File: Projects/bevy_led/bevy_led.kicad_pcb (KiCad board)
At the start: 2 copper layers, 66 x 61 mm, 78 parts, among them J1 USB_C_Receptacle_USB2.0, SW1 SW_Push, SW2 SW_Push, SW3 SW_Push, SW4 SW_Push, U1 DRTR5V0U4S, U2 ESP32-S3-MINI-1, U3 74AHCT1G125, U4 XC6222B331MR-G

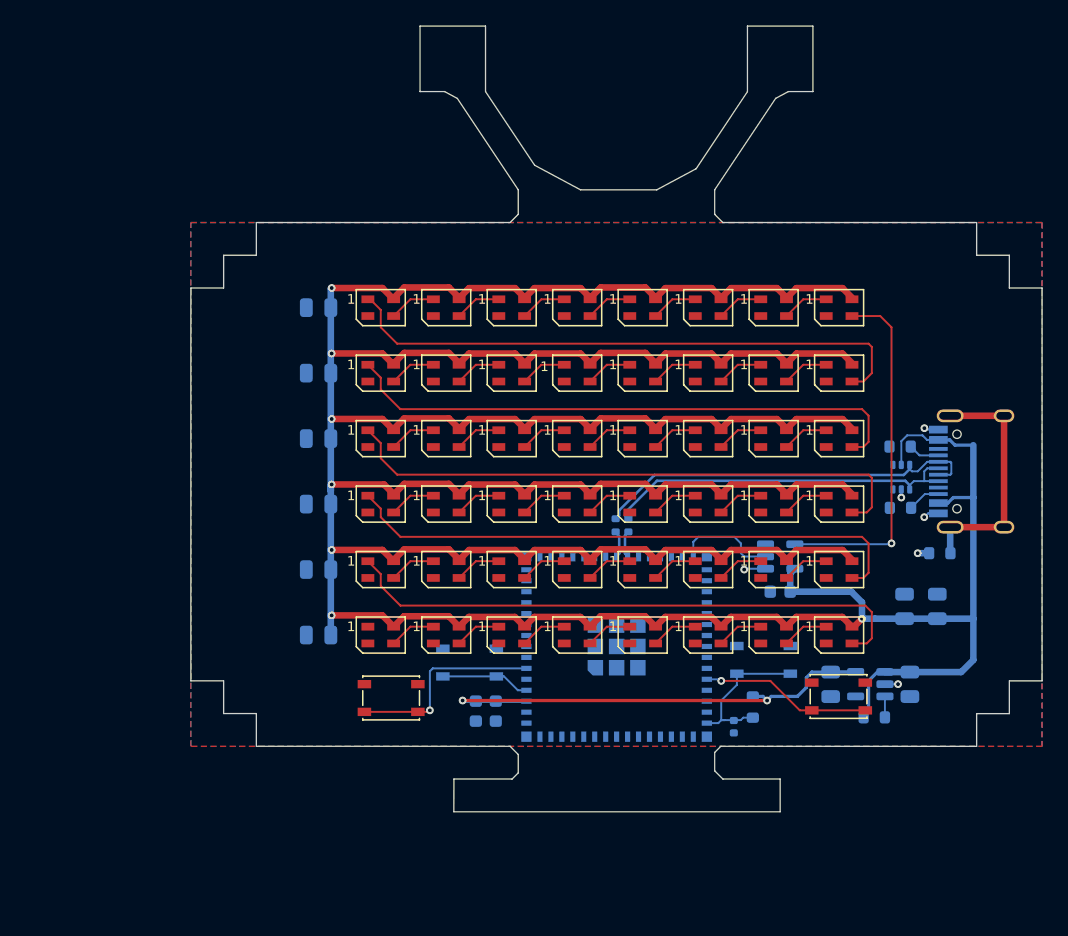
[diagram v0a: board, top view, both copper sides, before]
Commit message: Update board outline and add SAO header
TODO: figure out how to power from SAO or add battery.

Signed-off-by: Michael Welling <mwelling79@gmail.com>
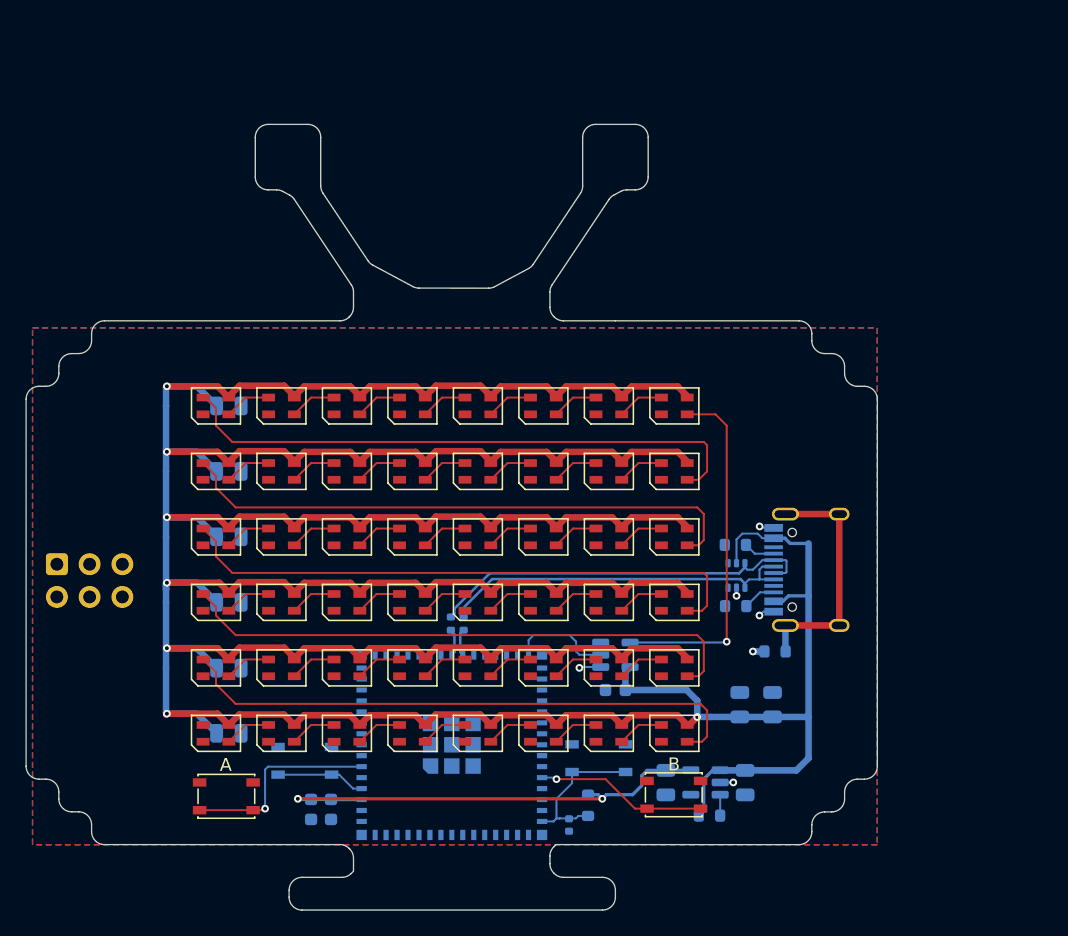
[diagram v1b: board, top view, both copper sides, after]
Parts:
- added J2: Conn_02x03_Odd_Even, Connector_IDC:IDC-Header_2x03_P2.54mm_Vertical, B.Cu at (109.0, 102.7)
- moved C5 14.9 mm to (156.2, 119.7)
- moved C6 14.9 mm to (152.3, 112.5)
- moved D34 14.9 mm to (151.8, 110.7)
- moved D37 14.9 mm to (136.6, 110.7)
- moved D42 14.9 mm to (151.8, 115.8)
- moved D45 14.9 mm to (136.6, 115.8)
- moved SW2 14.9 mm to (128.2, 118.0)
- moved U1 14.9 mm to (161.7, 103.6)
- moved C13 14.9 mm to (162.0, 113.6)
- moved D10 14.9 mm to (151.8, 95.5)
- moved D13 14.9 mm to (136.6, 95.5)
- moved D18 14.9 mm to (151.8, 100.6)
- moved D2 14.9 mm to (151.8, 90.4)
- moved D21 14.9 mm to (136.6, 100.6)
- moved D26 14.9 mm to (151.8, 105.7)
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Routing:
- net VBUS: track 357.1 -> 382.6 mm
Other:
- outline, holes or cut-outs redrawn
- board text added: "A"
- board text added: "B"
- board text added: "BOOT"
- board text added: "NRST"

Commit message: Update to sane LED ordering
Signed-off-by: Michael Welling <mwelling79@gmail.com>
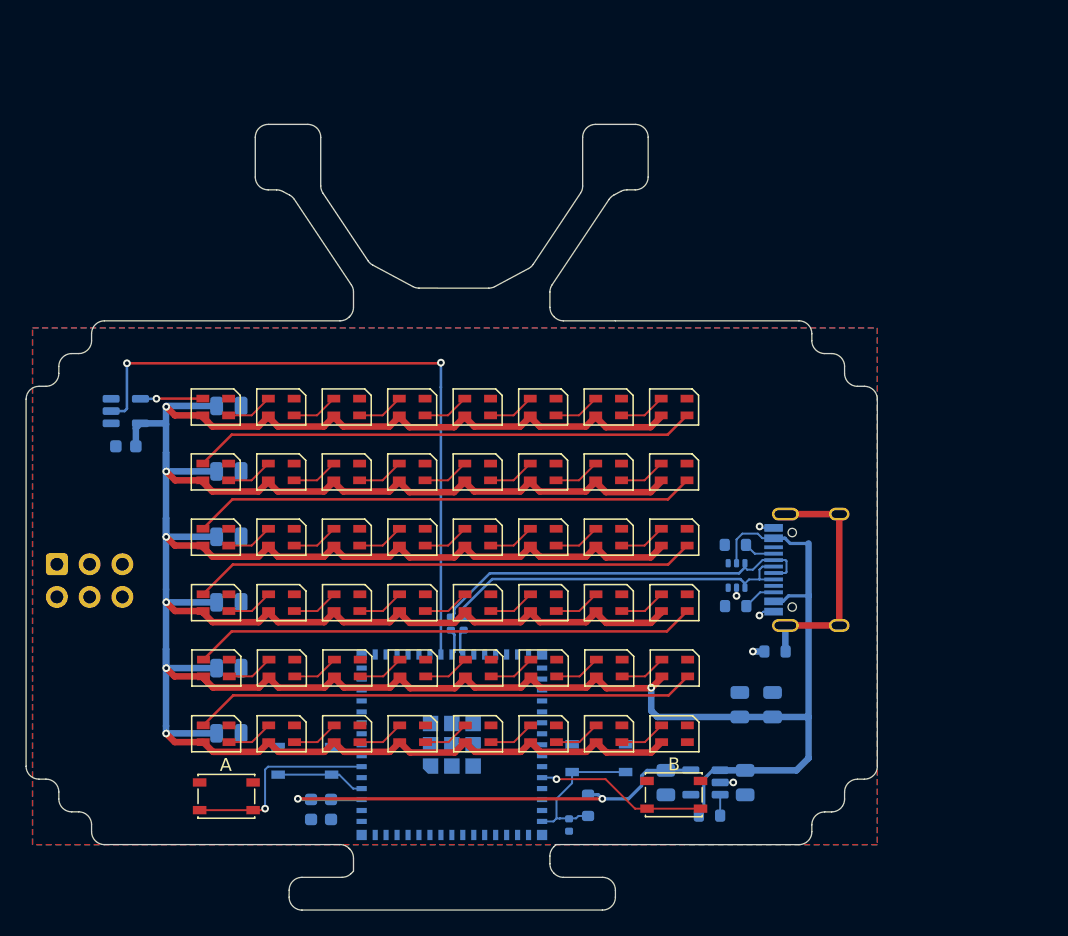
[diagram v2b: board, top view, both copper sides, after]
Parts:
- moved U3 42.4 mm to (114.3, 90.8)
- moved C6 42.4 mm to (114.3, 93.6)
- moved D40 35.6 mm to (156.9, 110.8), turned to 180 degrees
- moved D1 35.6 mm to (121.3, 90.5), turned to 180 degrees
- moved D9 35.6 mm to (121.3, 95.5), turned to 180 degrees
- moved D48 35.6 mm to (156.9, 115.9), turned to 180 degrees
- moved D17 35.6 mm to (121.3, 100.6), turned to 180 degrees
- moved D32 35.6 mm to (156.9, 105.7), turned to 180 degrees
- moved D25 35.6 mm to (121.3, 105.7), turned to 180 degrees
- moved D24 35.6 mm to (156.9, 100.6), turned to 180 degrees
- moved D41 35.5 mm to (121.3, 115.9), turned to 180 degrees
- moved D8 35.5 mm to (156.9, 90.5), turned to 180 degrees
- moved D16 35.5 mm to (156.9, 95.5), turned to 180 degrees
- moved D33 35.5 mm to (121.4, 110.8), turned to 180 degrees
- moved D39 25.4 mm to (151.8, 110.8), turned to 180 degrees
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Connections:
- U2 pad 22: unconnected-(U2-IO18-Pad22) -> /LED_IN
- U2 pad 30: /LED_IN -> unconnected-(U2-IO48-Pad30)
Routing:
- net /LED_IN: track 7.96 -> 51.9 mm, vias 0 -> 2
- net Net-(D1-DIN): track 27.7 -> 4.85 mm
- net VBUS: track 382.6 -> 372.1 mm
- net Net-(D24-DOUT): track 45.3 -> 39.1 mm
- net Net-(D8-DOUT): track 45.3 -> 39.3 mm
- net Net-(D40-DOUT): track 45.0 -> 39.2 mm
- net Net-(D32-DOUT): track 44.5 -> 39.1 mm
- net Net-(D16-DOUT): track 44.5 -> 39.1 mm
- net GND: track 6.57 -> 4.89 mm, vias 6 -> 5
